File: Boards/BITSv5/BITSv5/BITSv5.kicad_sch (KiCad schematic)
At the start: 97 parts, among them J2 USB_C_Receptacle_USB2.0, J3 SOICbite, J4 Conn_01x20, Q1 Q_NMOS_GSD, SW3 SLIDE, U1 MCU_RaspberryPi_RP2040_RP2040, U10 USBLC6-2SC6, U11 MS5607-02BA, U2 W25Q128JVS, U3 MAX-M10S, U4 DRF1262TL, U5 LT8653SIV-PBF, U6 TPS2121RUXR, U8 LT6703CDC-3, U9 TVS1800DRVR, Y1 12MHz

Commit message: changed BITSv5 antennas to ufl, added TIMEPULSE and EXTINT GPIOs, and exposed GPIO UART over header
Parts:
- removed AE1: Antenna, BITSv5:ANT_1575AT_JOT-M, symbol Device:Antenna
- removed AE2: Antenna, BITSv5:ANT_0915AT43A0026E_JOT, symbol Device:Antenna
- removed J4: Conn_01x20, symbol Connector_Generic:Conn_01x20
- added B1: KMR2, Button_Switch_SMD:SW_Push_1P1T_NO_CK_KMR2, symbol Switch:SW_Push
- added J1: Conn_01x03_Pin, Connector_PinHeader_2.54mm:PinHeader_1x03_P2.54mm_Vertical, symbol Connector:Conn_01x03_Pin
- added J4: Conn_01x10_Pin, Connector_Molex:Molex_PicoBlade_53261-1071_1x10-1MP_P1.25mm_Horizontal, symbol Connector:Conn_01x10_Pin
- added J5, J6: U.FL, Connector_Coaxial:U.FL_Molex_MCRF_73412-0110_Vertical, symbol Connector:Conn_Coaxial
- added R2: 10k, Resistor_SMD:R_0603_1608Metric, symbol Device:R_Small
- J2: footprint Connector_USB:USB_C_Receptacle_GCT_USB4085 -> Connector_USB:USB_C_Receptacle_GCT_USB4105-xx-A_16P_TopMnt_Horizontal
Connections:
- net +3V3: now also R2.1
- net +5V: now also J4.8 (Pin_8)
- net GND: now also B1.1, J1.3 (Pin_3), J4.10 (Pin_10), J5.2 (Ext), J6.2 (Ext)
- net IRIDIUM_CTS: now also J4.2 (Pin_2)
- net IRIDIUM_NETAV: now also J4.4 (Pin_4)
- net IRIDIUM_RING: now also J4.5 (Pin_5)
- net IRIDIUM_RTS: now also J4.3 (Pin_3)
- net IRIDIUM_RXD: now also J4.1 (Pin_1)
- net IRIDIUM_TXD: now also J4.6 (Pin_6)
- net at U3.11 (RF_IN): now also J5.1 (In)
- net at U3.2 (TXD): now also J1.2 (Pin_2)
- net at U3.3 (RXD): now also J1.1 (Pin_1)
- net at U4.16 (ANT): now also J6.1 (In)
- net RESET: no longer names the net of U1.26 (RUN)
- net RESET: now also B1.2, R2.2; no longer U4.10 (RST)
- net WATCHDOG renamed RDIO_RST
- net RDIO_RST: now also U4.10 (RST)
- new net: U3.10 (GND), U3.12 (GND)
- no-connect marks 36 -> 29
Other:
- moved on the sheet: H1, H2, H4, R21, R24

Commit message: BITSv5.1 ready for review
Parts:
- added C30: 100nF, Capacitor_SMD:C_0603_1608Metric, symbol Device:C_Small
- added U7: MB85RS1MT, BPP_Lib:BGA8CP30X40_5X3_309X228X35B25N, symbol Memory_NVRAM:MB85RS1MT
- U10: footprint SOT23-6L_STM -> BITSv5:SOT23-6L_STM
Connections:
- net +3V3: now also C30.1, U7.E3 (VDD)
- net +BATT: now also BT1.2 (+); no longer BT1.1 (+)
- net GND: now also BT1.1 (-), C30.2, U7.A1 (GND); no longer BT1.2 (-)
- net FRAM_CS: now reaches U1.41 (GPIO29_ADC3)
- net FRAM_CS: now also U7.E1 (~{CS})
- net DRF_CLK renamed SCK
- net SCK: now also U7.C3 (SCK)
- net DRF_MISO renamed MISO
- net MISO: now also U7.C1 (SO)
- net DRF_MOSI renamed MOSI
- net MOSI: now also U7.A3 (SI)
- new net: U3.10 (GND), U3.12 (GND)
- no-connect marks 29 -> 30
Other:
- note added: "FRAM"
- title: UMDBPP Command BITSv5 -> UMDBPP Command BITSv5.1

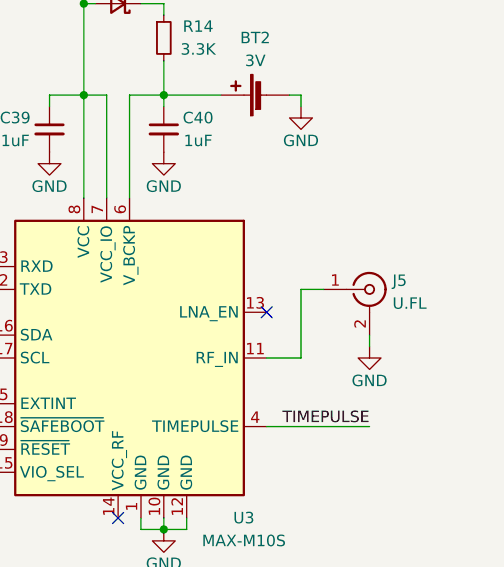
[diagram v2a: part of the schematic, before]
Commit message: nvm I want BITSv5 to have a chip antenna
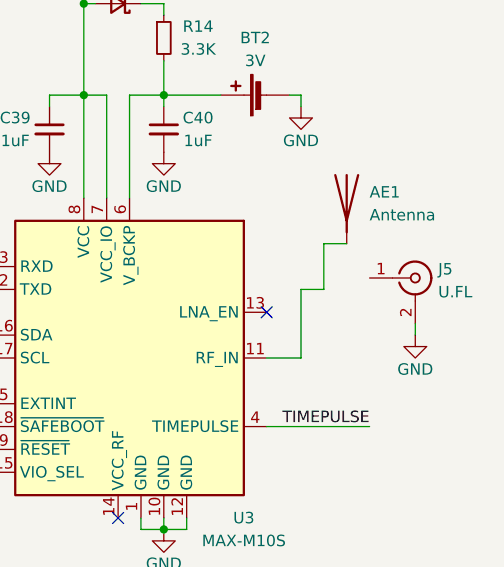
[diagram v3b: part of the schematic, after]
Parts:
- added AE1: Antenna, BPP_Lib:ANT_1575AT_JOT-M, symbol Device:Antenna
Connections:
- net at U3.11 (RF_IN): now also AE1.1 (A); no longer J5.1 (In)
- new net: U3.10 (GND), U3.12 (GND)
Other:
- moved on the sheet: J5
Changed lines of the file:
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@@
     (stroke (width 0) (type default))
   )
-  (wire (pts (xy 400.05 205.74) (xy 400.05 204.47))
+  (wire (pts (xy 405.13 204.47) (xy 405.13 203.2))
     (stroke (width 0) (type default))
   )
@@
     (stroke (width 0) (type default))
   )
+  (wire (pts (xy 394.97 199.39) (xy 394.97 194.31))
+    (stroke (width 0) (type default))
+  )
   (wire (pts (xy 199.39 45.72) (xy 199.39 44.45))
     (stroke (width 0) (type default))
@@
     (stroke (width 0) (type default))
   )
+  (wire (pts (xy 394.97 194.31) (xy 397.51 194.31))
+    (stroke (width 0) (type default))
+  )
   (wire (pts (xy 125.73 34.29) (xy 132.08 34.29))
     (stroke (width 0) (type default))
@@
     )
   )
-  (symbol (lib_id "power:GND") (at 400.05 205.74 0) (unit 1)
+  (symbol (lib_id "power:GND") (at 405.13 204.47 0) (unit 1)
     (in_bom yes) (on_board yes) (dnp no)
-    (property "Reference" "#PWR036" (at 400.05 212.09 0)
+    (property "Reference" "#PWR036" (at 405.13 210.82 0)
       (effects (font (size 1.27 1.27)) hide)
     )
-    (property "Value" "GND" (at 400.05 209.55 0)
+    (property "Value" "GND" (at 405.13 208.28 0)
       (effects (font (size 1.27 1.27)))
     )
-    (property "Footprint" "" (at 400.05 205.74 0)
+    (property "Footprint" "" (at 405.13 204.47 0)
       (effects (font (size 1.27 1.27)) hide)
     )
-    (property "Datasheet" "" (at 400.05 205.74 0)
+    (property "Datasheet" "" (at 405.13 204.47 0)
       (effects (font (size 1.27 1.27)) hide)
     )
@@
     )
   )
+  (symbol (lib_id "Device:Antenna") (at 397.51 189.23 0) (unit 1)
+    (in_bom yes) (on_board yes) (dnp no) (fields_autoplaced)
+    (property "Reference" "AE1" (at 400.05 188.595 0)
+      (effects (font (size 1.27 1.27)) (justify left))
+    )
+    (property "Value" "Antenna" (at 400.05 191.135 0)
+      (effects (font (size 1.27 1.27)) (justify left))
+    )
+    (property "Footprint" "BPP_Lib:ANT_1575AT_JOT-M" (at 397.51 189.23 0)
+      (effects (font (size 1.27 1.27)) hide)
+    )
+    (property "Datasheet" "~" (at 397.51 189.23 0)
+      (effects (font (size 1.27 1.27)) hide)
+    )
+    (pin "1")
+    (instances
+      (project "BITSv5"
+        (path "/55a258d3-b7da-466a-a6cc-38d8142826fc"
+          (reference "AE1") (unit 1)
+        )
+      )
+    )
+  )
   (symbol (lib_id "power:GND") (at 275.59 44.45 0) (unit 1)
     (in_bom yes) (on_board yes) (dnp no) (fields_autoplaced)
@@
     )
   )
-  (symbol (lib_id "Connector:Conn_Coaxial") (at 400.05 199.39 0) (unit 1)
+  (symbol (lib_id "Connector:Conn_Coaxial") (at 405.13 198.12 0) (unit 1)
     (in_bom yes) (on_board yes) (dnp no) (fields_autoplaced)
-    (property "Reference" "J5" (at 402.59 198.4132 0)
+    (property "Reference" "J5" (at 407.67 197.1432 0)
       (effects (font (size 1.27 1.27)) (justify left))
     )
-    (property "Value" "U.FL" (at 402.59 200.9532 0)
+    (property "Value" "U.FL" (at 407.67 199.6832 0)
       (effects (font (size 1.27 1.27)) (justify left))
     )
-    (property "Footprint" "Connector_Coaxial:U.FL_Molex_MCRF_73412-0110_Vertical" (at 400.05 199.39 0)
+    (property "Footprint" "Connector_Coaxial:U.FL_Molex_MCRF_73412-0110_Vertical" (at 405.13 198.12 0)
       (effects (font (size 1.27 1.27)) hide)
     )
-    (property "Datasheet" " ~" (at 400.05 199.39 0)
+    (property "Datasheet" " ~" (at 405.13 198.12 0)
       (effects (font (size 1.27 1.27)) hide)
     )

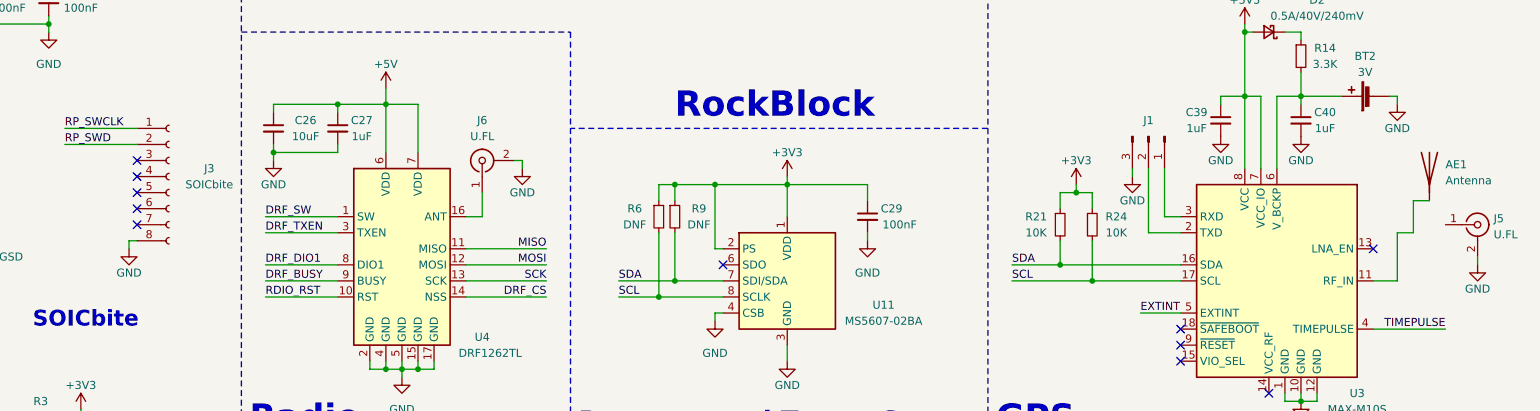
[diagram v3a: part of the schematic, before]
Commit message: finished GPS chip antenna, removed SOICbite for test points because couldn't find space
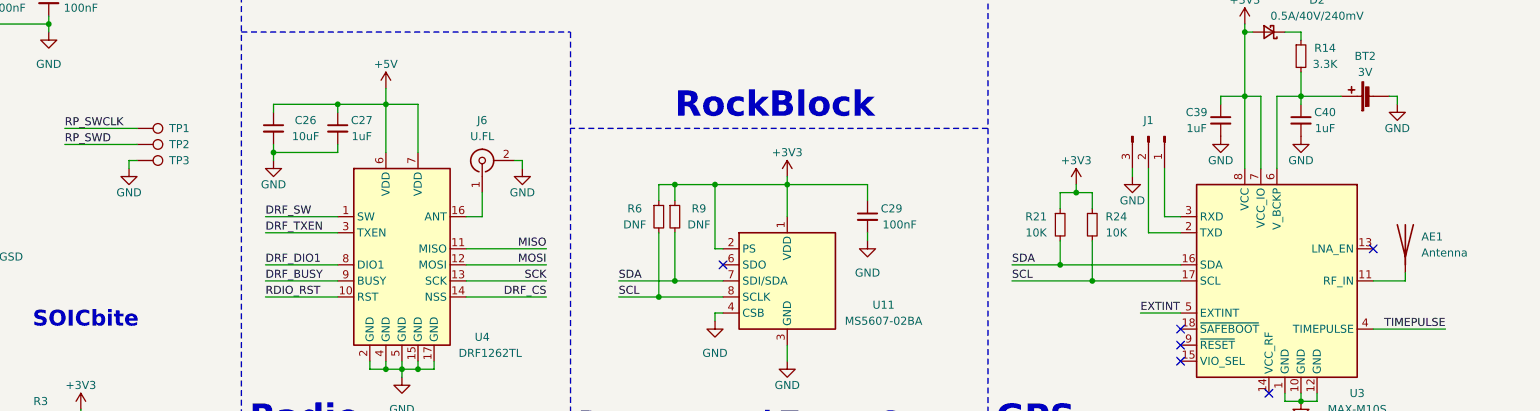
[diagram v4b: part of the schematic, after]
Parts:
- removed J3: SOICbite, BITSv5:SOIC_clipProgSmall, symbol Connector:Conn_01x08_Socket
- removed J5: U.FL, Connector_Coaxial:U.FL_Molex_MCRF_73412-0110_Vertical, symbol Connector:Conn_Coaxial
- added TP1, TP2, TP3: TestPoint, TestPoint:TestPoint_Pad_D2.0mm, symbol Connector:TestPoint
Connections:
- net GND: now also TP3.1
- net RP_SWCLK: now also TP1.1
- net RP_SWD: now also TP2.1
- new net: U3.10 (GND), U3.12 (GND)
- no-connect marks 30 -> 25
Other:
- moved on the sheet: AE1

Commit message: clean up
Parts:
- removed H1: M2, MountingHole:MountingHole_2.2mm_M2_Pad, symbol Mechanical:MountingHole
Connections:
- new net: U3.10 (GND), U3.12 (GND)
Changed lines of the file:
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@@
-    )
-  )
-  (symbol (lib_id "Mechanical:MountingHole") (at 162.56 274.32 0) (unit 1)
-    (in_bom yes) (on_board yes) (dnp no) (fields_autoplaced)
-    (property "Reference" "H1" (at 165.1 273.685 0)
-      (effects (font (size 1.27 1.27)) (justify left))
-    )
-    (property "Value" "M2" (at 165.1 276.225 0)
-      (effects (font (size 1.27 1.27)) (justify left))
-    )
-    (property "Footprint" "MountingHole:MountingHole_2.2mm_M2_Pad" (at 162.56 274.32 0)
-      (effects (font (size 1.27 1.27)) hide)
-    )
-    (property "Datasheet" "~" (at 162.56 274.32 0)
-      (effects (font (size 1.27 1.27)) hide)
-    )
-    (instances
-      (project "BITSv5"
-        (path "/55a258d3-b7da-466a-a6cc-38d8142826fc"
-          (reference "H1") (unit 1)
-        )
-      )
     )
   )

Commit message: BITSv5.1 ready for order, Gerbers generated
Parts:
- J4: value Conn_01x10_Pin -> PicoBlade_53261-1071
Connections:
- new net: U3.10 (GND), U3.12 (GND)
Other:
- moved on the sheet: J4
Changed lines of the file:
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@@
   (no_connect (at 101.6 236.22))
   (no_connect (at 101.6 261.62))
-  (no_connect (at 322.58 138.43))
+  (no_connect (at 297.18 165.1))
   (no_connect (at 340.36 88.9))
   (no_connect (at 285.75 204.47))
@@
   (no_connect (at 356.87 31.75))
   (no_connect (at 101.6 228.6))
-  (no_connect (at 322.58 133.35))
+  (no_connect (at 297.18 160.02))
   (no_connect (at 358.14 214.63))
   (no_connect (at 41.91 50.8))
@@
     (stroke (width 0) (type default))
   )
-  (wire (pts (xy 304.8 125.73) (xy 322.58 125.73))
+  (wire (pts (xy 279.4 152.4) (xy 297.18 152.4))
     (stroke (width 0) (type default))
   )
@@
     (stroke (width 0) (type default))
   )
-  (wire (pts (xy 304.8 123.19) (xy 322.58 123.19))
+  (wire (pts (xy 279.4 149.86) (xy 297.18 149.86))
     (stroke (width 0) (type default))
   )
@@
     (stroke (width 0) (type default))
   )
-  (wire (pts (xy 304.8 128.27) (xy 322.58 128.27))
+  (wire (pts (xy 279.4 154.94) (xy 297.18 154.94))
     (stroke (width 0) (type default))
   )
@@
     (stroke (width 0) (type default))
   )
+  (polyline (pts (xy 261.62 138.43) (xy 261.62 167.64))
+    (stroke (width 0) (type dash_dot))
+  )
   (wire (pts (xy 90.17 158.75) (xy 90.17 160.02))
     (stroke (width 0) (type default))
@@
     (stroke (width 0) (type default))
   )
-  (wire (pts (xy 321.31 140.97) (xy 322.58 140.97))
+  (wire (pts (xy 295.91 167.64) (xy 297.18 167.64))
     (stroke (width 0) (type default))
   )
@@
     (stroke (width 0) (type default))
   )
-  (wire (pts (xy 304.8 118.11) (xy 322.58 118.11))
+  (wire (pts (xy 279.4 144.78) (xy 297.18 144.78))
     (stroke (width 0) (type default))
   )
@@
     (stroke (width 0) (type default))
   )
-  (wire (pts (xy 304.8 120.65) (xy 322.58 120.65))
+  (wire (pts (xy 279.4 147.32) (xy 297.18 147.32))
     (stroke (width 0) (type default))
   )
@@
     (stroke (width 0) (type default))
   )
+  (polyline (pts (xy 327.66 138.43) (xy 261.62 138.43))
+    (stroke (width 0) (type dash_dot))
+  )
   (wire (pts (xy 43.18 160.02) (xy 43.18 158.75))
     (stroke (width 0) (type default))
@@
     (stroke (width 0) (type default))
   )
-  (wire (pts (xy 304.8 130.81) (xy 322.58 130.81))
+  (wire (pts (xy 279.4 157.48) (xy 297.18 157.48))
     (stroke (width 0) (type default))
   )
@@
     (stroke (width 0) (type default))
   )
-  (wire (pts (xy 300.99 135.89) (xy 322.58 135.89))
+  (wire (pts (xy 275.59 162.56) (xy 297.18 162.56))
     (stroke (width 0) (type default))
   )
@@
     (stroke (width 0) (type default))
   )
-  (wire (pts (xy 321.31 142.24) (xy 321.31 140.97))
+  (wire (pts (xy 295.91 168.91) (xy 295.91 167.64))
     (stroke (width 0) (type default))
   )
@@
     (stroke (width 0) (type default))
   )
-  (wire (pts (xy 300.99 135.89) (xy 300.99 134.62))
+  (wire (pts (xy 275.59 162.56) (xy 275.59 161.29))
     (stroke (width 0) (type default))
   )
@@
     (stroke (width 0) (type default))
   )
+  (polyline (pts (xy 327.66 157.48) (xy 327.66 138.43))
+    (stroke (width 0) (type dash_dot))
+  )
   (wire (pts (xy 214.63 180.34) (xy 214.63 179.07))
     (stroke (width 0) (type default))
@@
     (effects (font (size 4 4) (thickness 0.8) bold) (justify left bottom))
   )
-  (text "RockBlock" (at 278.13 181.61 0)
+  (text "RockBlock" (at 262.89 181.61 0)
     (effects (font (size 4 4) (thickness 0.8) bold) (justify left bottom))
   )
@@
     (effects (font (size 1.27 1.27)) (justify right bottom))
   )
-  (label "IRIDIUM_CTS" (at 304.8 120.65 0) (fields_autoplaced)
+  (label "IRIDIUM_CTS" (at 279.4 147.32 0) (fields_autoplaced)
     (effects (font (size 1.27 1.27)) (justify left bottom))
   )
@@
     (effects (font (size 1.27 1.27)) (justify right bottom))
   )
-  (label "IRIDIUM_RTS" (at 304.8 123.19 0) (fields_autoplaced)
+  (label "IRIDIUM_RTS" (at 279.4 149.86 0) (fields_autoplaced)
     (effects (font (size 1.27 1.27)) (justify left bottom))
   )
@@
     (effects (font (size 1.27 1.27)) (justify left bottom))
   )
-  (label "IRIDIUM_RXD" (at 304.8 118.11 0) (fields_autoplaced)
+  (label "IRIDIUM_RXD" (at 279.4 144.78 0) (fields_autoplaced)
     (effects (font (size 1.27 1.27)) (justify left bottom))
   )
@@
     (effects (font (size 1.27 1.27)) (justify left bottom))
   )
-  (label "IRIDIUM_RING" (at 304.8 128.27 0) (fields_autoplaced)
+  (label "IRIDIUM_RING" (at 279.4 154.94 0) (fields_autoplaced)
     (effects (font (size 1.27 1.27)) (justify left bottom))
   )
@@
     (effects (font (size 1.27 1.27)) (justify right bottom))
   )
-  (label "IRIDIUM_NETAV" (at 304.8 125.73 0) (fields_autoplaced)
+  (label "IRIDIUM_NETAV" (at 279.4 152.4 0) (fields_autoplaced)
     (effects (font (size 1.27 1.27)) (justify left bottom))
   )
@@
     (effects (font (size 1.27 1.27)) (justify right bottom))
   )
-  (label "IRIDIUM_TXD" (at 304.8 130.81 0) (fields_autoplaced)
+  (label "IRIDIUM_TXD" (at 279.4 157.48 0) (fields_autoplaced)
     (effects (font (size 1.27 1.27)) (justify left bottom))
   )
@@
     )
   )
-  (symbol (lib_id "Connector:Conn_01x10_Pin") (at 327.66 128.27 0) (mirror y) (unit 1)
+  (symbol (lib_id "Connector:Conn_01x10_Pin") (at 302.26 154.94 0) (mirror y) (unit 1)
     (in_bom yes) (on_board yes) (dnp no)
-    (property "Reference" "J4" (at 328.93 130.81 0)
+    (property "Reference" "J4" (at 303.53 157.48 0)
       (effects (font (size 1.27 1.27)) (justify right))
     )
-    (property "Value" "Conn_01x10_Pin" (at 328.93 128.27 0)
+    (property "Value" "PicoBlade_53261-1071" (at 303.53 154.94 0)
       (effects (font (size 1.27 1.27)) (justify right))
     )
-    (property "Footprint" "Connector_Molex:Molex_PicoBlade_53261-1071_1x10-1MP_P1.25mm_Horizontal" (at 327.66 128.27 0)
+    (property "Footprint" "Connector_Molex:Molex_PicoBlade_53261-1071_1x10-1MP_P1.25mm_Horizontal" (at 302.26 154.94 0)
       (effects (font (size 1.27 1.27)) hide)
     )
-    (property "Datasheet" "~" (at 327.66 128.27 0)
+    (property "Datasheet" "~" (at 302.26 154.94 0)
       (effects (font (size 1.27 1.27)) hide)
     )
@@
     )
   )
-  (symbol (lib_id "power:GND") (at 321.31 142.24 0) (unit 1)
+  (symbol (lib_id "power:GND") (at 295.91 168.91 0) (unit 1)
     (in_bom yes) (on_board yes) (dnp no)
-    (property "Reference" "#PWR050" (at 321.31 148.59 0)
+    (property "Reference" "#PWR050" (at 295.91 175.26 0)
       (effects (font (size 1.27 1.27)) hide)
     )
-    (property "Value" "GND" (at 321.31 146.05 0)
+    (property "Value" "GND" (at 295.91 172.72 0)
       (effects (font (size 1.27 1.27)))
     )
-    (property "Footprint" "" (at 321.31 142.24 0)
+    (property "Footprint" "" (at 295.91 168.91 0)
       (effects (font (size 1.27 1.27)) hide)
     )
-    (property "Datasheet" "" (at 321.31 142.24 0)
+    (property "Datasheet" "" (at 295.91 168.91 0)
       (effects (font (size 1.27 1.27)) hide)
     )
@@
     )
   )
-  (symbol (lib_id "power:+5V") (at 300.99 134.62 0) (unit 1)
+  (symbol (lib_id "power:+5V") (at 275.59 161.29 0) (unit 1)
     (in_bom yes) (on_board yes) (dnp no) (fields_autoplaced)
-    (property "Reference" "#PWR018" (at 300.99 138.43 0)
+    (property "Reference" "#PWR018" (at 275.59 165.1 0)
       (effects (font (size 1.27 1.27)) hide)
     )
-    (property "Value" "+5V" (at 300.99 130.81 0)
+    (property "Value" "+5V" (at 275.59 157.48 0)
       (effects (font (size 1.27 1.27)))
     )
-    (property "Footprint" "" (at 300.99 134.62 0)
+    (property "Footprint" "" (at 275.59 161.29 0)
       (effects (font (size 1.27 1.27)) hide)
     )
-    (property "Datasheet" "" (at 300.99 134.62 0)
+    (property "Datasheet" "" (at 275.59 161.29 0)
       (effects (font (size 1.27 1.27)) hide)
     )

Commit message: starting power changes for BITSv5.2
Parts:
- removed BT1: 1S1P LiPo, Connector_AMASS:AMASS_XT30PW-M_1x02_P2.50mm_Horizontal, symbol Device:Battery_Cell
- removed C17, C23: 4.7pF, Capacitor_SMD:C_0603_1608Metric, symbol Device:C_Small
- removed C18, C21: 470pF, Capacitor_SMD:C_0603_1608Metric, symbol Device:C_Small
- removed C19, C24: 10nF, Capacitor_SMD:C_0603_1608Metric, symbol Device:C_Small
- removed C20: 47uF, Capacitor_SMD:C_1206_3216Metric, symbol Device:C_Small
- removed C22: 100nF, Capacitor_SMD:C_0603_1608Metric, symbol Device:C_Small
- removed C25, C36: 1uF, Capacitor_SMD:C_0603_1608Metric, symbol Device:C_Small
- removed C35: 10uF, Capacitor_SMD:C_0603_1608Metric, symbol Device:C_Small
- removed L1, L2: 2.2uH, Inductor_SMD:L_1210_3225Metric, symbol Device:L_Small
- removed R15: 23.7K, Resistor_SMD:R_0603_1608Metric, symbol Device:R_Small
- removed R16: 5K, Resistor_SMD:R_0603_1608Metric, symbol Device:R_Small
- removed R32: 34.8K, Resistor_SMD:R_0603_1608Metric, symbol Device:R_Small
- removed R33: 100K, Resistor_SMD:R_0603_1608Metric, symbol Device:R_Small
- removed R34: 15K, Resistor_SMD:R_0603_1608Metric, symbol Device:R_Small
- removed U5: LT8653SIV-PBF, BITSv5:LT8653SIV-PBF, symbol BITSv5:LT8653SIV-PBF
- added J3: XT30, symbol Connector_Generic:Conn_01x02
- added R25: 10.2k, symbol Device:R_Small
- added R26: 5k, symbol Device:R_Small
- added R28: 0, symbol Device:R_Small
- added R30: 47.5k, symbol Device:R_Small
- added TP4, TP5: TestPoint, symbol Connector:TestPoint
- C15: value 4.7uF -> 10uF
- C16: value 47uF -> 1uF; footprint Capacitor_SMD:C_1206_3216Metric -> (none)
- C33: value 10nF -> 1uF
- R22: value 23.7K -> DNF; footprint Resistor_SMD:R_0603_1608Metric -> (none)
- R23: value 5K -> 0; footprint Resistor_SMD:R_0603_1608Metric -> (none)
- R27: value 22.1K -> DNF; footprint Resistor_SMD:R_0603_1608Metric -> (none)
- R29: value 100K -> 15k; footprint Resistor_SMD:R_0603_1608Metric -> (none)
- TP3: footprint TestPoint:TestPoint_Pad_D2.0mm -> (none)
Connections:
- net +3V3: now also TP5.1
- net +5V: now also TP4.1
- net +BATT: now also J3.2 (Pin_2); no longer C34.1, R22.1, U6.2 (IN2)
- net GND: now also J3.1 (Pin_1), R26.2, R28.2, R30.2; no longer U6.3 (CP2), U6.6 (PR1)
- net VBUS: now also C15.1, R22.1, R29.1; no longer J2.A4 (VBUS), J2.A9 (VBUS), J2.B4 (VBUS), J2.B9 (VBUS), U10.5
- net at R27.2: now also U6.4 (OV2), R28.1
- net at R22.2, R23.1: now also U6.5 (OV1); no longer U6.4 (OV2)
- net at R27.1: now also C34.1, U6.2 (IN2), R25.1
- net at C16.1, L4.2, R13.2: now also U6.1 (OUT), U6.8 (OUT); no longer R29.1
- net at R29.2: now also U6.6 (PR1), R30.1
- net VCC: no longer names the net of C37.1, R18.1, R20.1, U8.2 (V+)
- net VCC: no longer C15.1, U6.1 (OUT), U6.8 (OUT)
- new net: R25.2, R26.1, U6.3 (CP2)
- new net: U3.10 (GND), U3.12 (GND)
- new net: J2.A4 (VBUS), J2.A9 (VBUS), J2.B4 (VBUS), J2.B9 (VBUS), U10.5
- no-connect marks 25 -> 22
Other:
- note added: "Finish calculating switchover resistor values"
- note added: "TPSM33625FRDNR"
- note removed: "5V / 3.3V Buck Regulator"
- moved on the sheet: C28, C30, C33, C34, C37, C38, L3, L4, R10, R13, R17, R18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
